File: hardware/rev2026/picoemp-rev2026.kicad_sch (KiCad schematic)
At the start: 47 parts, among them J1 Header 7, J2 1x2_Pin_Header, J3 BG306-02-A-2-0400-L-G, J4 Header 2, J5 Header 4, J6 EDGE-SMA, Q1 LDA111STR, Q2 RGT16BM65DTL, Q3 AO3422, Q4 AO3422, SW1 KSC741J LFS, SW2 KSC741J LFS, SW3 TL3301AF160QJ, T1 ATB322524, T2 ATB322524, U1 SC0915

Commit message: Flatten Altium value variables, normalize BOM fields, fix R9 part data
Structural rewrite via the Task 1 s-expression parser and property_span()
(tools/normalize_fields.py) instead of the plan's regex approach -- a
parenthesis inside a property value would silently corrupt an s-expression
edited with blind regex. Flattens ${ALTIUM_VALUE} to each symbol's literal
value, renames MANUFACTURE PART NUMBER 1/MANUFACTURER_PART_NUMBER -> MPN,
MANUFACTURE 1/MANUFACTURER_NAME -> Manufacturer, SUPPLIER PART NUMBER 1 ->
DigiKey, and deletes 33 kinds of Altium/distributor cruft fields (PART
NUMBER, COMPONENT GROUP/KIND/TYPE, PP ROTATION, SNAPEDA_LINK, etc). Verified
against the pre-edit netlist export: same 64 nets, same (ref, pin) node set
on every net, same 150 total nodes -- only property blocks changed.

R9's value is 2k but every part field carried R4's 75R data
(RCHIP-75R-0805 / RC0805FR-0775RL / 311-75.0CRCT-ND). This is an
upstream defect in the Altium source; the published .xls BOM has the
correct RC0805FR-072KL / 311-2.00KCRCT-ND. C5 had no value at all
upstream; set to 100n per the design spec.

Backfilled MPN/Manufacturer/DigiKey for the remaining retained parts from
design spec sections 5.2/5.3 (C1-C3, D1-D5, D2, D7, D8/LED2, Q1, Q2, Q3/Q4,
T1/T2, U1, J2, and the future-J1 SMA connector currently ref J6), including
correcting J2's corrupted duplicate-string Molex placeholder to the spec's
JST S2B-XH-A(LF)(SN). Left LED1/LED3 (D6/D9 substitution) and SW1-3 (switch
family TBD) without MPN -- both are open items assigned to later tasks, not
oversights; bom_manager.py analyze confirms exactly these 3 BOM lines lack
MPN. Re-ran the LCSC datasheet sync with the newly populated MPNs; all 19
real MPNs (including ATB322524-0110-T000 and LDA111STR) came back with no
LCSC hit, so datasheet coverage is unchanged at 1/24 (U1 only) -- Task 6's
direct-URL fallback will be needed for those two.

Co-Authored-By: Claude Opus 5 <noreply@anthropic.com>
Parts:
- C1, C2: DigiKey (none) -> 445-5980-1-ND; MPN (none) -> C2012X5R1H475K125AB; Manufacturer (none) -> TDK
- C3: DigiKey (none) -> 490-16845-1-ND; MPN (none) -> KRM55TR72J474MH01K; Manufacturer (none) -> Murata
- C5: value ${ALTIUM_VALUE} -> 100n; DigiKey (none) -> 399-5089-2-ND; MPN (none) -> C0603C104K5RACTU; Manufacturer (none) -> KEMET
- D1, D3, D4, D5: DigiKey (none) -> SM4005PL-TPMSCT-ND; MPN (none) -> SM4005PL-TP; Manufacturer (none) -> MCC
- D2: MPN (none) -> MURA160T3G; Manufacturer (none) -> onsemi
- D7: DigiKey (none) -> MM3Z18VBCT-ND; MPN (none) -> MM3Z18VB; Manufacturer (none) -> onsemi
- J1: LATESTREVISIONDATE 17-Jul-2002 -> (none); LATESTREVISIONNOTE Re-released for DXP Platform. -> (none); PUBLISHER Altium Limited -> (none)
- J2: COMPONENT GROUP Connector -> (none); COMPONENT KIND Standard -> (none); COMPONENT TYPE Standard -> (none); DigiKey (none) -> 455-2257-ND; MANUFACTURE 1 Molex -> (none); MANUFACTURE PART NUMBER 1 22-23-2021 22-23-2021 -> (none); MOUNTING TECHNOLOGY Through-hole -> (none); MPN (none) -> S2B-XH-A(LF)(SN); Manufacturer (none) -> JST; PART NUMBER Molex_2_Pin -> (none); PIN COUNT 2 -> (none); PP MATERIAL STACK 0 -> (none); PP ROTATION 0 -> (none); ROHS Yes -> (none); SUPPLIER 1 Digi-Key -> (none); SUPPLIER PART NUMBER 1 WM4200-ND -> (none)
- J6: MPN (none) -> 132289; Manufacturer (none) -> Amphenol
- LED2: DigiKey (none) -> 754-1116-1-ND; MPN (none) -> APT1608CGCK; Manufacturer (none) -> Kingbright
- MH1, MH2, MH3: COMPONENT GROUP Mechanical -> (none); COMPONENT KIND Mechanical -> (none); COMPONENT TYPE Mechanical -> (none); PART NUMBER MOUNT_M3_TIGHT -> (none); PIN COUNT 1 -> (none); PP MATERIAL STACK 0 -> (none); PP ROTATION 0 -> (none)
- Q1: ARROW PART NUMBER LDA111STR -> (none); ARROW PRICE/STOCK https://www.arrow.com/en/products/lda111str/ixys -> (none); DATASHEET LINK https://datasheet.datasheetarchive.com/originals/dk/DKDS-13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 -> (none); DigiKey (none) -> 212-LDA111SCT-ND; HEIGHT 4.699mm -> (none); MANUFACTURER_NAME IXYS SEMICONDUCTOR -> (none); MANUFACTURER_PART_NUMBER LDA111STR -> (none); MOUSER PART NUMBER 849-LDA111STR -> (none); MOUSER PRICE/STOCK https://www.mouser.co.uk/ProductDetail/IXYS-Integrated-Circ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 -> (none); MPN (none) -> LDA111STR; Manufacturer (none) -> IXYS SEMICONDUCTOR
- Q2: MPN (none) -> RGT16BM65DTL; Manufacturer (none) -> ROHM
- Q3, Q4: MPN (none) -> AO3422
- R1: value ${ALTIUM_VALUE} -> 20M; ALTIUM_VALUE 20M -> (none); CASE-EIA 2010 -> (none); CASE-METRIC 5025 -> (none); COMPONENT GROUP Resistor -> (none); COMPONENT KIND Standard -> (none); COMPONENT TYPE Standard -> (none); MANUFACTURE 1 Vishay -> (none); MANUFACTURE PART NUMBER 1 CRMA2010AF20M0FKEF -> (none); MOUNTING TECHNOLOGY SMT -> (none); MPN (none) -> CRMA2010AF20M0FKEF; Manufacturer (none) -> Vishay; PART NUMBER RCHIP-20M-2010 -> (none); PIN COUNT 2 -> (none); RATED POWER 0.5W -> (none); RATED VOLTAGE 400VDC -> (none); SUPPLIER 1 Digi-Key -> (none); TEMPERATURE RANGE -55C to 155C -> (none); TOLERANCE 1% -> (none)
- R10, R11, R12, R13, R5: value ${ALTIUM_VALUE} -> 1k; ALTIUM_VALUE 1k -> (none); CASE-EIA 0603 -> (none); CASE-METRIC 1608 -> (none); COMPONENT GROUP Resistor -> (none); COMPONENT KIND Standard -> (none); COMPONENT TYPE Standard -> (none); DigiKey (none) -> 311-1.00KHRCT-ND; MANUFACTURE 1 Yageo -> (none); MANUFACTURE PART NUMBER 1 RC0603FR-071KL -> (none); MOUNTING TECHNOLOGY SMT -> (none); MPN (none) -> RC0603FR-071KL; Manufacturer (none) -> Yageo; PART NUMBER RCHIP-1K-0603 -> (none); PIN COUNT 2 -> (none); RATED POWER 0.1W -> (none); RATED VOLTAGE 75VDC -> (none); SUPPLIER 1 Digi-Key -> (none); SUPPLIER PART NUMBER 1 311-1.00KHRCT-ND -> (none); TEMPERATURE RANGE -55C to 155C -> (none); TOLERANCE 1% -> (none)
- R2: value ${ALTIUM_VALUE} -> 300K; ALTIUM_VALUE 300K -> (none); CASE-EIA 2512 -> (none); CASE-METRIC 6432 -> (none); COMPONENT GROUP Resistor -> (none); COMPONENT KIND Standard -> (none); COMPONENT TYPE Standard -> (none); DigiKey (none) -> A121215CT-ND; MANUFACTURE 1 TE Connectivity -> (none); MANUFACTURE PART NUMBER 1 3522300KFT -> (none); MOUNTING TECHNOLOGY SMT -> (none); MPN (none) -> 3522300KFT; Manufacturer (none) -> TE Connectivity; PART NUMBER RCHIP-300K-2512 -> (none); PIN COUNT 2 -> (none); RATED POWER 3W -> (none); RATED VOLTAGE 250V -> (none); ROHS Yes -> (none); SUPPLIER 1 Digi-Key -> (none); SUPPLIER PART NUMBER 1 A121215CT-ND -> (none); TEMPERATURE RANGE -55C to 155C -> (none); TOLERANCE 1% -> (none)
- R3, R7: value ${ALTIUM_VALUE} -> 10R; ALTIUM_VALUE 10R -> (none); CASE-EIA 0603 -> (none); CASE-METRIC 1608 -> (none); COMPONENT GROUP Resistor -> (none); COMPONENT KIND Standard -> (none); COMPONENT TYPE Standard -> (none); DigiKey (none) -> 311-10.0HRCT-ND; MANUFACTURE 1 Yageo -> (none); MANUFACTURE PART NUMBER 1 RC0603FR-0710RL -> (none); MOUNTING TECHNOLOGY SMT -> (none); MPN (none) -> RC0603FR-0710RL; Manufacturer (none) -> Yageo; PART NUMBER RCHIP-10R-0603 -> (none); PIN COUNT 2 -> (none); RATED POWER 0.1W -> (none); RATED VOLTAGE 75VDC -> (none); SUPPLIER 1 Digi-Key -> (none); SUPPLIER PART NUMBER 1 311-10.0HRCT-ND -> (none); TEMPERATURE RANGE -55C to 155C -> (none); TOLERANCE 1% -> (none)
- R4: ALTIUM_VALUE 75R -> (none); CASE-EIA 0805 -> (none); COMPONENT GROUP Resistor -> (none); COMPONENT KIND Standard -> (none); COMPONENT TYPE Standard -> (none); DigiKey (none) -> 311-75.0CRCT-ND; MANUFACTURE 1 Yageo -> (none); MANUFACTURE PART NUMBER 1 RC0805FR-0775RL -> (none); MOUNTING TECHNOLOGY SMT -> (none); MPN (none) -> RC0805FR-0775RL; Manufacturer (none) -> Yageo; PART NUMBER RCHIP-75R-0805 -> (none); PIN COUNT 2 -> (none); RATED POWER 0.125W -> (none); RATED VOLTAGE 75VDC -> (none); SUPPLIER 1 Digi-Key -> (none); SUPPLIER PART NUMBER 1 311-75.0CRCT-ND -> (none); TEMPERATURE RANGE -55C to 155C -> (none); TOLERANCE 1% -> (none)
- R6: value ${ALTIUM_VALUE} -> 22k; ALTIUM_VALUE 22k -> (none); CASE-EIA 0603 -> (none); CASE-METRIC 1608 -> (none); COMPONENT GROUP Resistor -> (none); COMPONENT KIND Standard -> (none); COMPONENT TYPE Standard -> (none); DigiKey (none) -> 311-22.0KHRCT-ND; MANUFACTURE 1 Yageo -> (none); MANUFACTURE PART NUMBER 1 RC0603FR-0722KL -> (none); MOUNTING TECHNOLOGY SMT -> (none); MPN (none) -> RC0603FR-0722KL; Manufacturer (none) -> Yageo; PART NUMBER RCHIP-22K-0603 -> (none); PIN COUNT 2 -> (none); RATED POWER 0.1W -> (none); RATED VOLTAGE 75VDC -> (none); SUPPLIER 1 Digi-Key -> (none); SUPPLIER PART NUMBER 1 311-22.0KHRCT-ND -> (none); TEMPERATURE RANGE -55C to 155C -> (none); TOLERANCE 1% -> (none)
- R9: ALTIUM_VALUE 75R -> (none); CASE-EIA 0805 -> (none); COMPONENT GROUP Resistor -> (none); COMPONENT KIND Standard -> (none); COMPONENT TYPE Standard -> (none); DigiKey (none) -> 311-2.00KCRCT-ND; MANUFACTURE 1 Yageo -> (none); MANUFACTURE PART NUMBER 1 RC0805FR-0775RL -> (none); MOUNTING TECHNOLOGY SMT -> (none); MPN (none) -> RC0805FR-072KL; Manufacturer (none) -> Yageo; PART NUMBER RCHIP-75R-0805 -> (none); PIN COUNT 2 -> (none); RATED POWER 0.125W -> (none); RATED VOLTAGE 75VDC -> (none); SUPPLIER 1 Digi-Key -> (none); SUPPLIER PART NUMBER 1 311-75.0CRCT-ND -> (none); TEMPERATURE RANGE -55C to 155C -> (none); TOLERANCE 1% -> (none)
- T1, T2: COMPONENT GROUP Inductor -> (none); COMPONENT KIND Standard -> (none); COMPONENT TYPE Standard -> (none); DigiKey (none) -> 445-8636-1-ND; MANUFACTURE 1 TDK -> (none); MANUFACTURE PART NUMBER 1 ATB322524 -> (none); MOUNTING TECHNOLOGY SMT -> (none); MPN (none) -> ATB322524-0110-T000; Manufacturer (none) -> TDK; PART NUMBER ATB322524_PROTO -> (none); PIN COUNT 4 -> (none); ROHS Yes -> (none); SUPPLIER 1 Mouser -> (none)
- U1: ALTIUM_VALUE * -> (none); AVAILABILITY In Stock -> (none); CHECK_PRICES https://www.snapeda.com/parts/SC0915/Raspberry%20Pi/view-pa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 -> (none); COMPONENT GROUP PCB Feature -> (none); COMPONENT KIND Standard -> (none); COMPONENT TYPE Standard -> (none); MF Raspberry Pi -> (none); MP SC0915 -> (none); MPN (none) -> SC0915; Manufacturer (none) -> Raspberry Pi; PACKAGE None -> (none); PART NUMBER SC0915 -> (none); PP MATERIAL STACK 0 -> (none); PP ROTATION 0 -> (none); PP ROTATION1 0 -> (none); PRICE None -> (none); PURCHASE-URL https://pricing.snapeda.com/search/part/SC0915/?ref=eda -> (none); SNAPEDA_LINK https://www.snapeda.com/parts/SC0915/Raspberry%20Pi/view-pa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 -> (none)

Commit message: Add missing Manufacturer on Q3/Q4 (AO3422)
Review finding: Q3/Q4 were the only two BOM symbols with an MPN but no
Manufacturer. Spec §5.2's row for AO3422 lists only the part number, no
maker, unlike every other bare-MPN row in this task (R1->Vishay,
R3-R7->Yageo, R2->TE Connectivity, T1/T2->TDK, Q2->ROHM) which I did fill
in. Set Manufacturer = Alpha & Omega Semiconductor, the AO3422's actual
maker (the "AO" prefix is that company's own numbering scheme). DigiKey
stays blank on both -- the spec has no DigiKey PN for this row, same as
Q2/R1/T1/T2.

Co-Authored-By: Claude Opus 5 <noreply@anthropic.com>
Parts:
- Q3, Q4: Manufacturer (none) -> Alpha & Omega Semiconductor
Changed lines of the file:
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@@
+			)
+		)
+		(property "Manufacturer" "Alpha & Omega Semiconductor" (at 0 0 0)
+			(effects
+				(font
+					(size 1.27 1.27)
+				)
+				(hide yes)
 			)
 		)
@@
 			(effects
 				(font
+					(size 1.27 1.27)
+				)
+				(hide yes)
+			)
+		)
+		(property "Manufacturer" "Alpha & Omega Semiconductor" (at 0 0 0)
+			(effects
+				(font

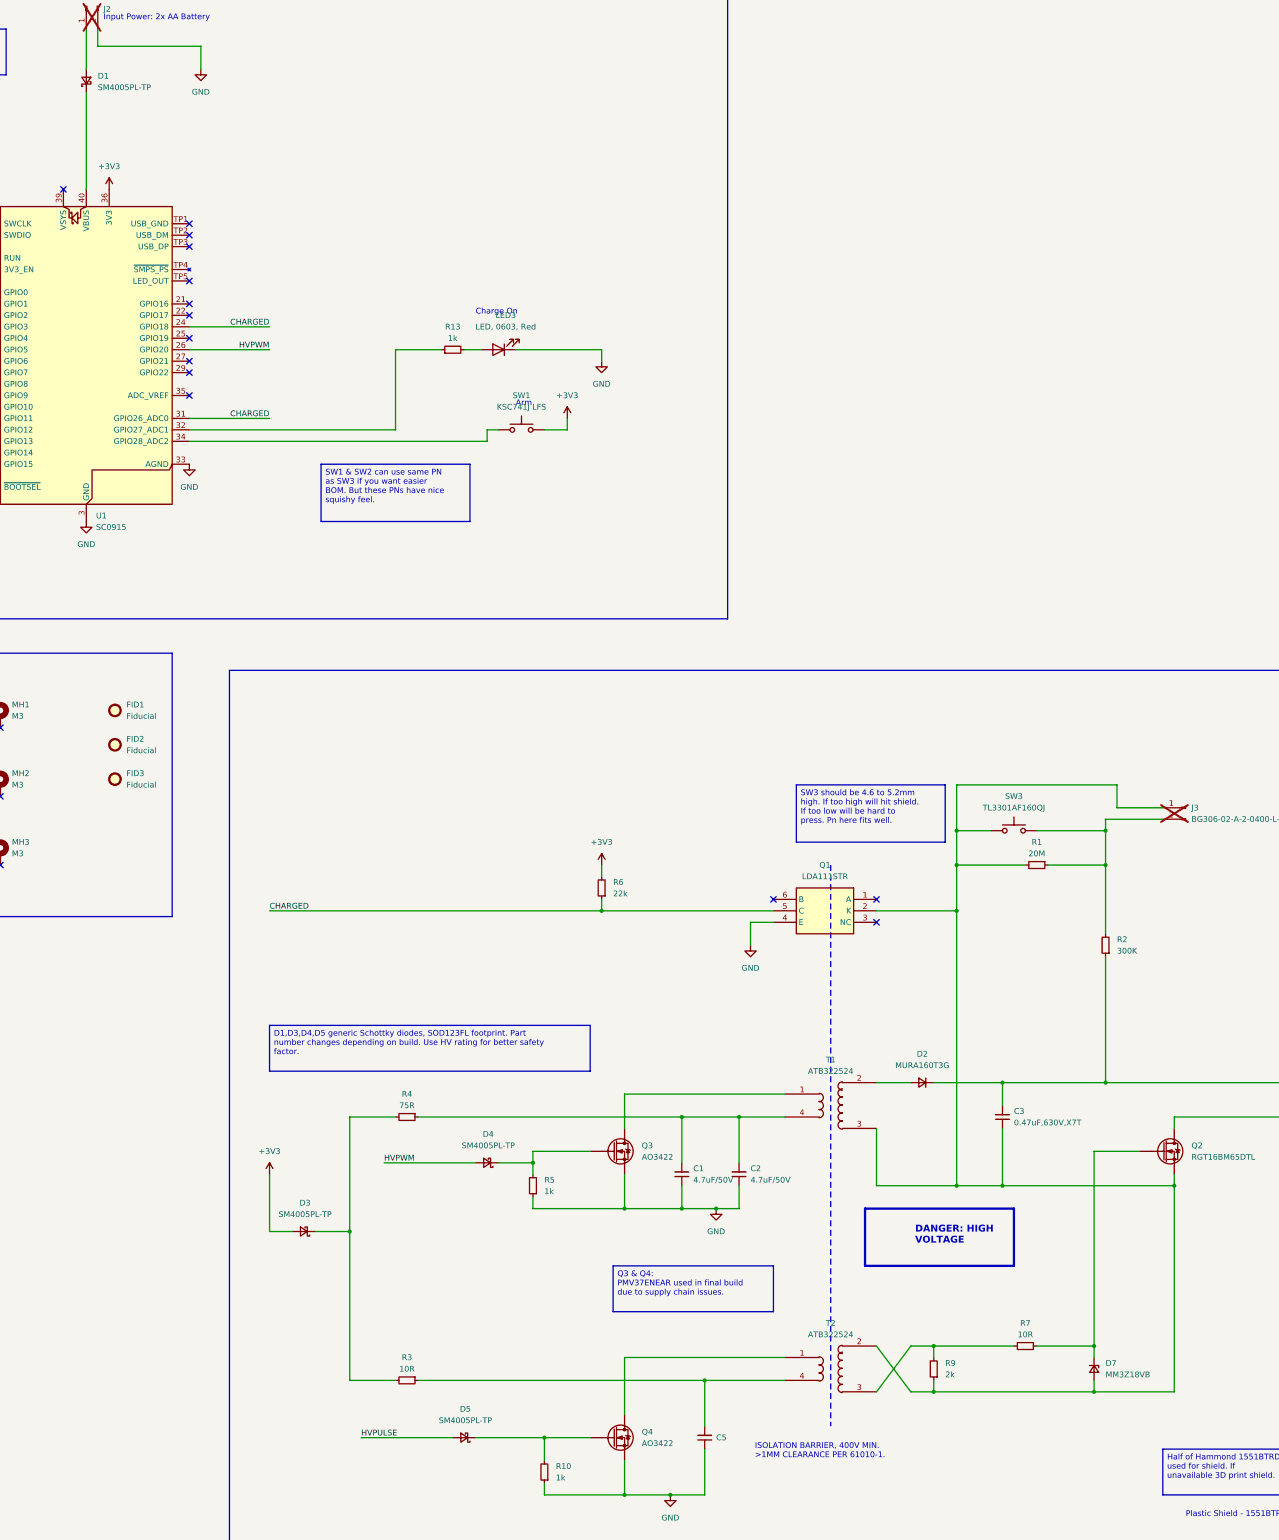
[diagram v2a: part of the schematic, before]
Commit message: Correct symbol classes: IGBT, enhancement MOSFETs, non-Schottky rectifiers
D1/D3/D4/D5 were drawn as Schottky diodes. This is a documented
upstream errata - hardware/README.md notes the schematic 'claimed they
were Schottky diodes, but as @settinger caught this was never the case'.

Q2 -> picoemp:IGBT_NCH_Diode, Q3/Q4 -> Transistor_FET:Q_NMOS_GSD,
Q1 -> picoemp:LDA111, T1/T2 -> new picoemp:ATB322524 (primary on pins
1/4, secondary on 2/3, matching this design's actual wiring rather than
Device:Transformer_1P_1S's 1/2+3/4 grouping). D1/D3/D4/D5 -> Device:D_Small.

Q2/Q3/Q4 pin numbering changes (D/G/S -> 1/2/3) required deliberate
per-uuid pin reconnection rather than a bare lib_id swap, verified
against a full netlist membership diff (64 nets before, 63 after;
every non-Q1/Q2/Q3/Q4 net is byte-identical; the only net that
disappears is Q1's legitimately-NC pin 3). Also rebuilt the
schematic's lib_symbols cache (kicad-cli resolves pin geometry from
this cache, not live sym-lib-table lookup, so new/changed lib_ids
need a cache entry too) and fixed LDA111's pin geometry, which Task 4
modeled on Isolator:4N25's layout rather than this schematic's actual
Altium-derived wiring for Q1.

Co-Authored-By: Claude Opus 5 <noreply@anthropic.com>
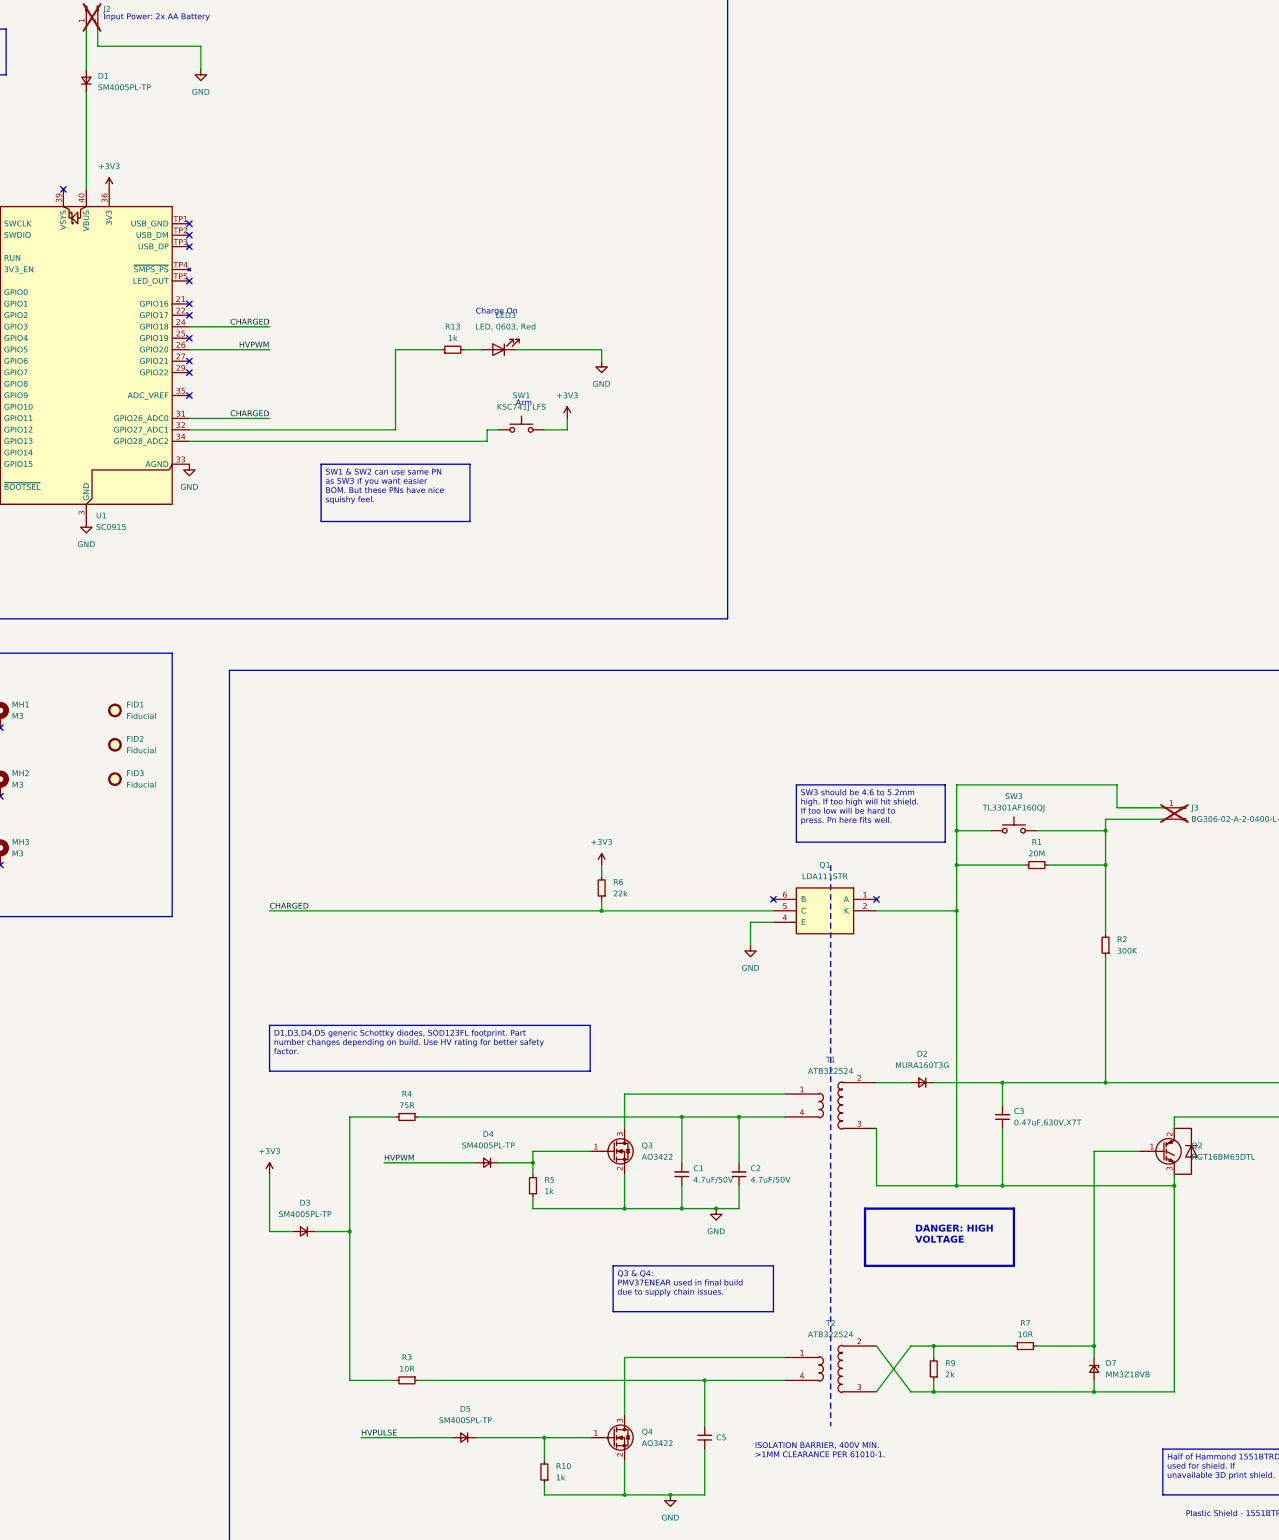
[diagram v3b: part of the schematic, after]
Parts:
- D1, D3, D4, D5: symbol Device:D_Schottky_Small -> Device:D_Small
- Q1: symbol *:root_0_mirrored_LDA111STR_* -> picoemp:LDA111
- Q2: symbol Device:Q_NMOS_Depletion -> picoemp:IGBT_NCH_Diode
- Q3, Q4: symbol Device:Q_NMOS_Depletion -> Transistor_FET:Q_NMOS_GSD
- T1, T2: symbol NewAE_AltiumLib:root_0_xformer_2_2_hv_NewAE_AltiumLib.DBLib -> picoemp:ATB322524
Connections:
- net GND: now also Q3.2 (S), Q4.2 (S); no longer Q3.S, Q4.S
- net at C3.1, D7.2 (A), J3.1 (Pin_1)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: now also Q2.3 (E); no longer Q2.S
- net at D4.1 (K), R5.2: now also Q3.1 (G); no longer Q3.G
- net at D5.1 (K), R10.2: now also Q4.1 (G); no longer Q4.G
- net at J6.2 (Ext): now also Q2.2 (C); no longer Q2.D
- net at D7.1 (K), R7.1: now also Q2.1 (G); no longer Q2.G
- net at T1.1: now also Q3.3 (D); no longer Q3.D
- net at T2.1: now also Q4.3 (D); no longer Q4.D
- no-connect marks 28 -> 27
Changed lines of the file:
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@@
 	)
 	(no_connect
-		(at 317.5 241.3)
-	)
-	(no_connect
 		(at 165.1 88.9)
 	)
@@
 	)
 	(symbol
-		(lib_id "Device:D_Schottky_Small")
+		(lib_id "Device:D_Small")
 		(at 190.5 309.88 180)
 		(unit 1)
@@
 			)
 		)
-		(property "Description" "Schottky diode, small symbol"
+		(property "Description" "Diode, small symbol"
 			(at 190.5 309.88 0)
 			(hide yes)
@@
 	)
 	(symbol
-		(lib_id "Device:D_Schottky_Small")
+		(lib_id "Device:D_Small")
 		(at 231.14 294.64 180)
 		(unit 1)
@@
 			)
 		)
-		(property "Description" "Schottky diode, small symbol"
+		(property "Description" "Diode, small symbol"
 			(at 231.14 294.64 0)
 			(hide yes)
@@
 	)
 	(symbol
-		(lib_id "Device:D_Schottky_Small")
+		(lib_id "Device:D_Small")
 		(at 226.06 355.6 180)
 		(unit 1)
@@
 			)
 		)
-		(property "Description" "Schottky diode, small symbol"
+		(property "Description" "Diode, small symbol"
 			(at 226.06 355.6 0)
 			(hide yes)
@@
 	)
 	(symbol
-		(lib_id "Device:Q_NMOS_Depletion")
+		(lib_id "picoemp:IGBT_NCH_Diode")
 		(at 381 292.1 0)
 		(unit 1)
@@
 			)
 		)
-		(property "Description" "Depletion-mode N-channel MOSFET"
+		(property "Description" "N-channel IGBT (TO-252/DPAK) with co-packed antiparallel diode, cathode at collector"
 			(at 381 292.1 0)
 			(hide yes)
@@
 			)
 		)
-		(pin "G"
+		(pin "1"
 		)
-		(pin "S"
+		(pin "3"
 		)
-		(pin "D"
+		(pin "2"
 		)
 		(instances
@@
 	)
 	(symbol
-		(lib_id "Device:Q_NMOS_Depletion")
+		(lib_id "Transistor_FET:Q_NMOS_GSD")
 		(at 259.08 292.1 0)
 		(unit 1)
@@
 			)
 		)
-		(property "Description" "Depletion-mode N-channel MOSFET"
+		(property "Description" "N-channel MOSFET, SOT-23, GSD pinout"
 			(at 259.08 292.1 0)
 			(hide yes)
@@
 			)
 		)
-		(pin "D"
+		(pin "3"
 		)
-		(pin "G"
+		(pin "1"
 		)
-		(pin "S"
+		(pin "2"
 		)
 		(instances
@@
 	)
 	(symbol
-		(lib_id "NewAE_AltiumLib:root_0_xformer_2_2_hv_NewAE_AltiumLib.DBLib")
+		(lib_id "picoemp:ATB322524")
 		(at 304.8 340.36 90)
 		(unit 1)
@@
 	)
 	(symbol
-		(lib_id "NewAE_AltiumLib:root_0_xformer_2_2_hv_NewAE_AltiumLib.DBLib")
+		(lib_id "picoemp:ATB322524")
 		(at 304.8 281.94 90)
 		(unit 1)
@@
 	)
 	(symbol
-		(lib_id "Device:Q_NMOS_Depletion")
+		(lib_id "Transistor_FET:Q_NMOS_GSD")
 		(at 259.08 355.6 0)
 		(unit 1)
@@
 			)
 		)
-		(property "Description" "Depletion-mode N-channel MOSFET"
+		(property "Description" "N-channel MOSFET, SOT-23, GSD pinout"
 			(at 259.08 355.6 0)
 			(hide yes)
@@
 			)
 		)
-		(pin "G"
+		(pin "1"
 		)
-		(pin "S"
+		(pin "2"
 		)
-		(pin "D"
+		(pin "3"
 		)
 		(instances
@@
 	)
 	(symbol
-		(lib_id "*:root_0_mirrored_LDA111STR_*")
+		(lib_id "picoemp:LDA111")
 		(at 317.5 236.22 270)
 		(mirror x)
@@
 		(pin "4"
 		)
-		(pin "3"
-		)
 		(instances
 			(project "ChipShouter-Pico"
@@
 	)
 	(symbol
-		(lib_id "Device:D_Schottky_Small")
+		(lib_id "Device:D_Small")
 		(at 142.24 54.61 90)
 		(unit 1)
@@
 			)
 		)
-		(property "Description" "Schottky diode, small symbol"
+		(property "Description" "Diode, small symbol"
 			(at 142.24 54.61 0)
 			(hide yes)
